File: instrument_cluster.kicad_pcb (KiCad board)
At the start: 2 copper layers, 99.1 x 45.7 mm, 82 parts, among them J1 Conn_02x16_Top_Bottom, J2 Conn_02x16_Top_Bottom, J3 USB mini-B SMD, J4 NOT_FITTED_SWD_Conn_01x04_Male, J5 54819-0572, J6 NOT_FITTED_SWD_Conn_01x04_Male, U1 LM2575S-5.0_NOPB, U10 74HC4050D, U11 TJA1040T, U12 TJA1040T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

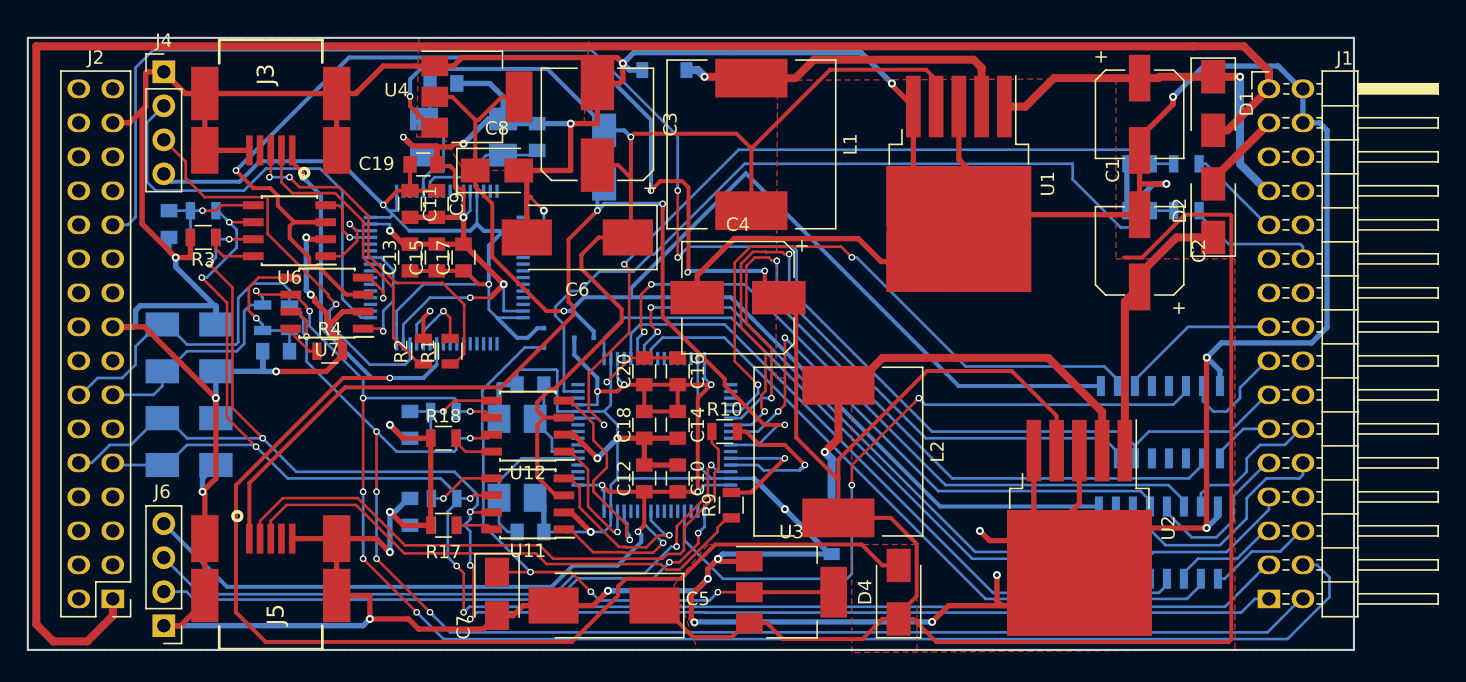
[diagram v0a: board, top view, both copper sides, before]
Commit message: fix signal trace length usb module A
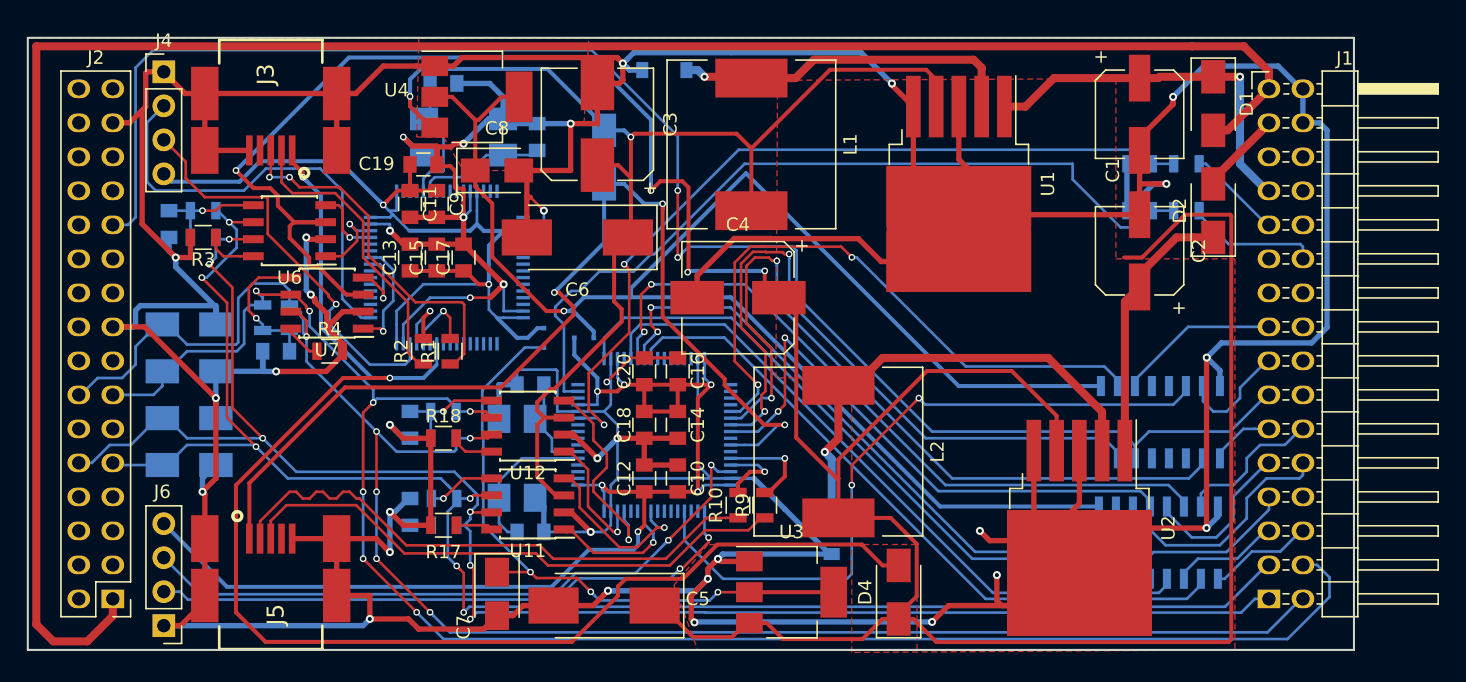
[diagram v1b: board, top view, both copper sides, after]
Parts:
- moved R10 5.59 mm to (161.0, 120.0), turned to 90 degrees
- moved R9 2.50 mm to (163.0, 120.0)
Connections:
- net Net-(J3-Pad2) renamed /Module A (2can_filter)/module_a_usb_D-
- net Net-(J3-Pad3) renamed /Module A (2can_filter)/module_a_usb_D+
- net Net-(J5-Pad2) renamed module_a_usb_D-
- net Net-(J5-Pad3) renamed module_a_usb_D+
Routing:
- net /Module B (2can_filter+extra)/USB_D-: track 13.5 -> 5.78 mm
- net module_a_usb_D-: track 46.0 -> 42.1 mm
- net /+5V_CAN-B: track 96.0 -> 92.7 mm
- net module_a_usb_D+: track 40.0 -> 42.0 mm
- net /Module B (2can_filter+extra)/USB_D+: track 9.11 -> 7.40 mm
- net /Module B (2can_filter+extra)/CAN2_TX: track 11.4 -> 10.3 mm
- net /USB_Vbus-B: track 75.6 -> 76.5 mm
- net /Module B (2can_filter+extra)/CAN2_RX: track 13.8 -> 13.0 mm
- net /Module B (2can_filter+extra)/SWCLK: track 44.5 -> 45.2 mm
- net /Module B (2can_filter+extra)/SWDIO: track 49.7 -> 49.1 mm
- net GND: vias 36 -> 35

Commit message: sch&pcb: add LED`s and refresh readme image`s
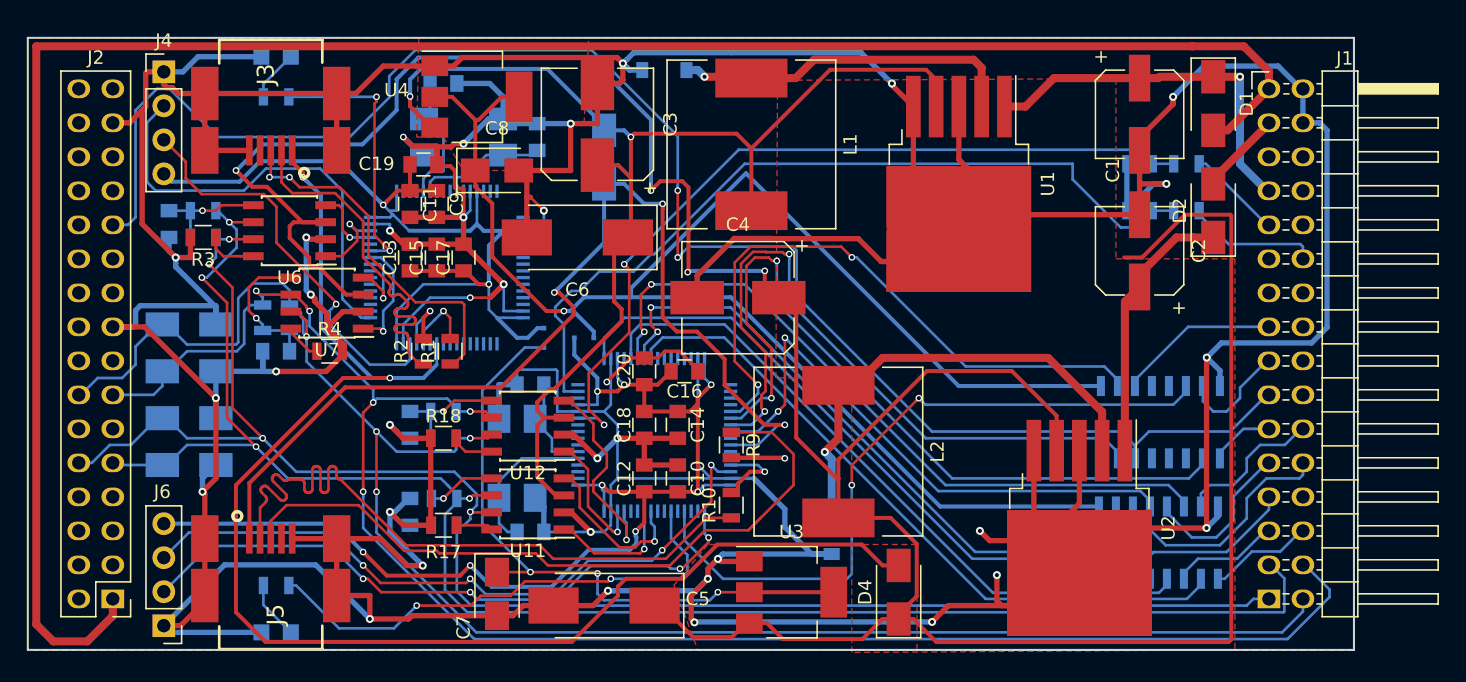
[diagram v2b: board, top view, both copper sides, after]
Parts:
- added D13: LED, LEDs:LED_0805, B.Cu at (126.5, 86.5)
- added D14: LED, LEDs:LED_0805, B.Cu at (126.5, 129.5)
- added R15: 1k, Resistors_SMD:R_0805, B.Cu at (126.5, 89.5)
- added R16: 10k, Resistors_SMD:R_0805, B.Cu at (126.5, 126.0)
- moved R9 5.15 mm to (160.5, 115.5), turned to 270 degrees
- moved C16 0.50 mm to (157.0, 110.0), turned to 0 degrees
- moved R10 0.50 mm to (160.5, 120.0)
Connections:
- net module_a_usb_D+ renamed Net-(J5-Pad3)
- net module_a_usb_D- renamed Net-(J5-Pad2)
- U5 pad 59: Net-(U5-Pad59) -> /Module A (2can_filter)/led_1
- U9 pad 54: Net-(U9-Pad54) -> /Module B (2can_filter+extra)/led_2
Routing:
- net /Module B (2can_filter+extra)/led_2: track 0.00 -> 37.9 mm, vias 0 -> 2
- net GND: track 665.1 -> 689.2 mm
- net /Module A (2can_filter)/led_1: track 0.00 -> 20.0 mm, vias 0 -> 2
- net Net-(J5-Pad3): track 42.0 -> 54.2 mm
- net Net-(J5-Pad2): track 42.1 -> 53.6 mm
- net /Module A (2can_filter)/module_a_usb_D-: track 22.4 -> 27.1 mm
- net Net-(D14-Pad2): track 0.00 -> 4.35 mm
- net /HS_CAN_L: track 125.1 -> 129.0 mm, vias 6 -> 4
- net Net-(D13-Pad2): track 0.00 -> 3.85 mm
- net /Module B (2can_filter+extra)/SWCLK: track 45.2 -> 48.1 mm, vias 2 -> 4
- net /ANTI-THEFT: track 121.0 -> 123.1 mm
- net /Module B (2can_filter+extra)/SWDIO: track 49.1 -> 51.1 mm, vias 2 -> 4
- net /MS_CAN_L: track 132.7 -> 130.8 mm, vias 7 -> 5
- net /+3V3_STM-B: track 91.8 -> 90.0 mm, vias 6 -> 8
- net /HS_CAN_H: track 125.8 -> 124.3 mm, vias 6 -> 4
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
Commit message: add gerbers files
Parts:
- J3, J5: footprint zulljon:USB_mini_B -> zpkl:USB_mini_B
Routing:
- net /+5V_CAN-A: track 223.5 -> 159.4 mm
- net /VBATT: track 151.1 -> 146.0 mm
- net /+3V3_LSH-B: track 121.6 -> 117.8 mm
- net GND: track 689.2 -> 691.9 mm, vias 35 -> 37
- net /+5V_CAN-B: track 92.7 -> 95.2 mm
- net /power_supply/+12V_A: track 20.3 -> 22.3 mm

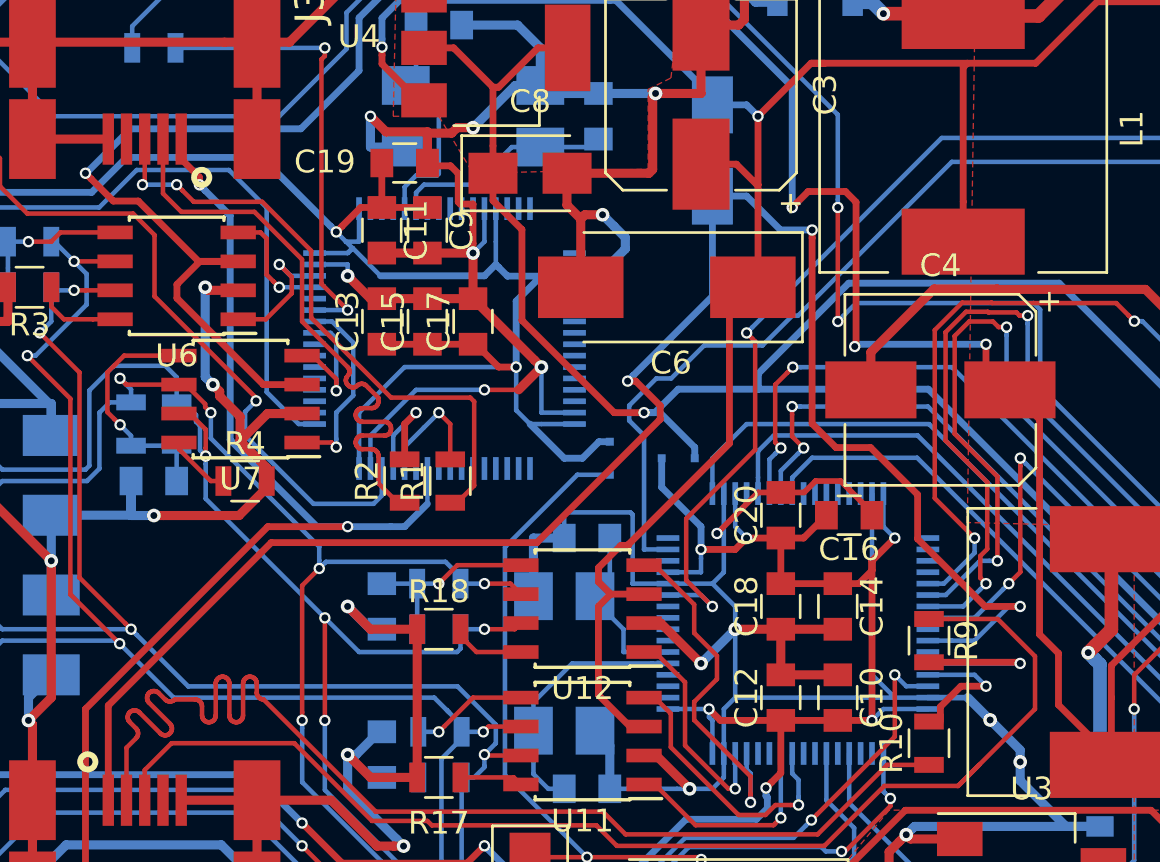
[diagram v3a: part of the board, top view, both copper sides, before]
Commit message: fix USB, swapped the traces D+ D-
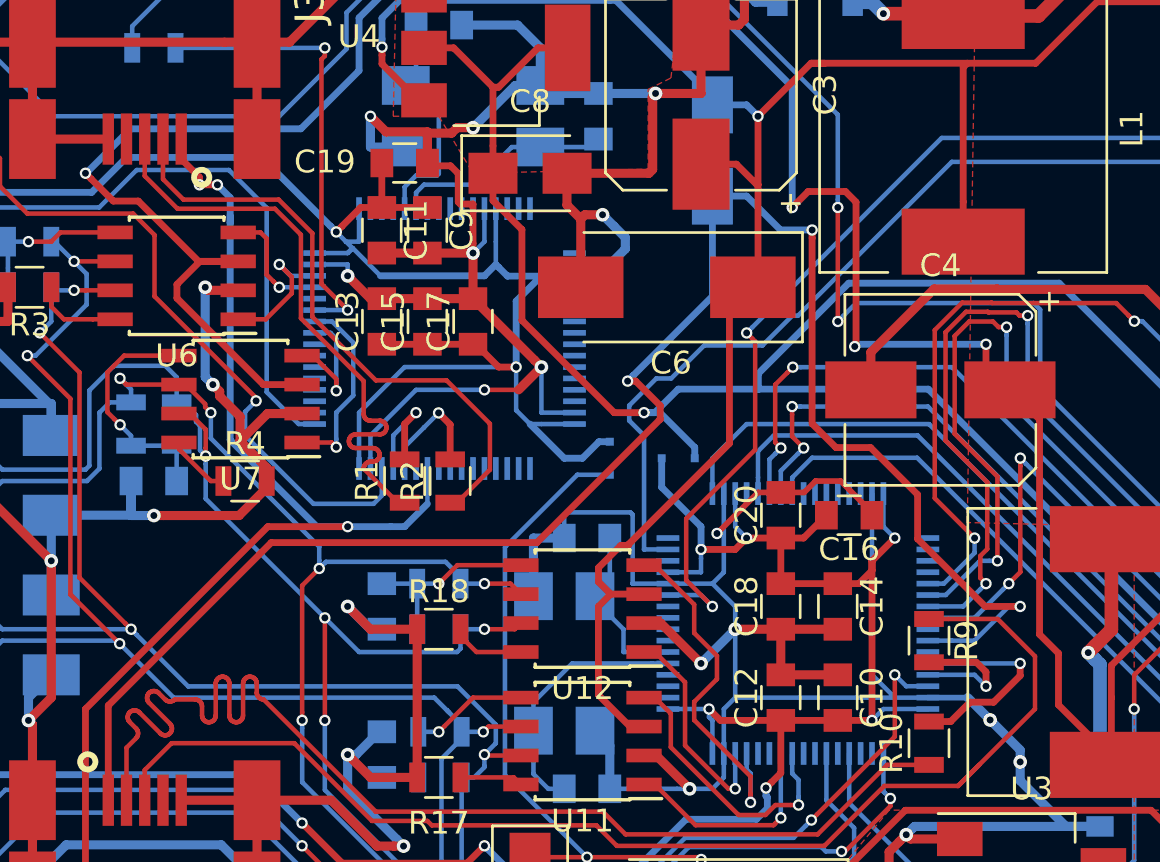
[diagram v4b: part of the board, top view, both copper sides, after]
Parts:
- moved R1 2.00 mm to (137.5, 108.5)
- moved R2 2.00 mm to (139.5, 108.5)
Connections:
- U5 pad 44: /Module A (2can_filter)/USB_D+ -> /Module A (2can_filter)/USB_D-
- U5 pad 45: /Module A (2can_filter)/USB_D- -> /Module A (2can_filter)/USB_D+
- U9 pad 44: /Module B (2can_filter+extra)/USB_D+ -> /Module B (2can_filter+extra)/USB_D-
- U9 pad 45: /Module B (2can_filter+extra)/USB_D- -> /Module B (2can_filter+extra)/USB_D+
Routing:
- net /Module B (2can_filter+extra)/USB_D-: track 5.78 -> 9.42 mm
- net /Module B (2can_filter+extra)/USB_D+: track 8.07 -> 6.06 mm
- net /USB_Vbus-A: track 104.8 -> 105.5 mm, vias 2 -> 3
- net /Module A (2can_filter)/module_a_usb_D+: track 27.3 -> 27.0 mm, vias 2 -> 0

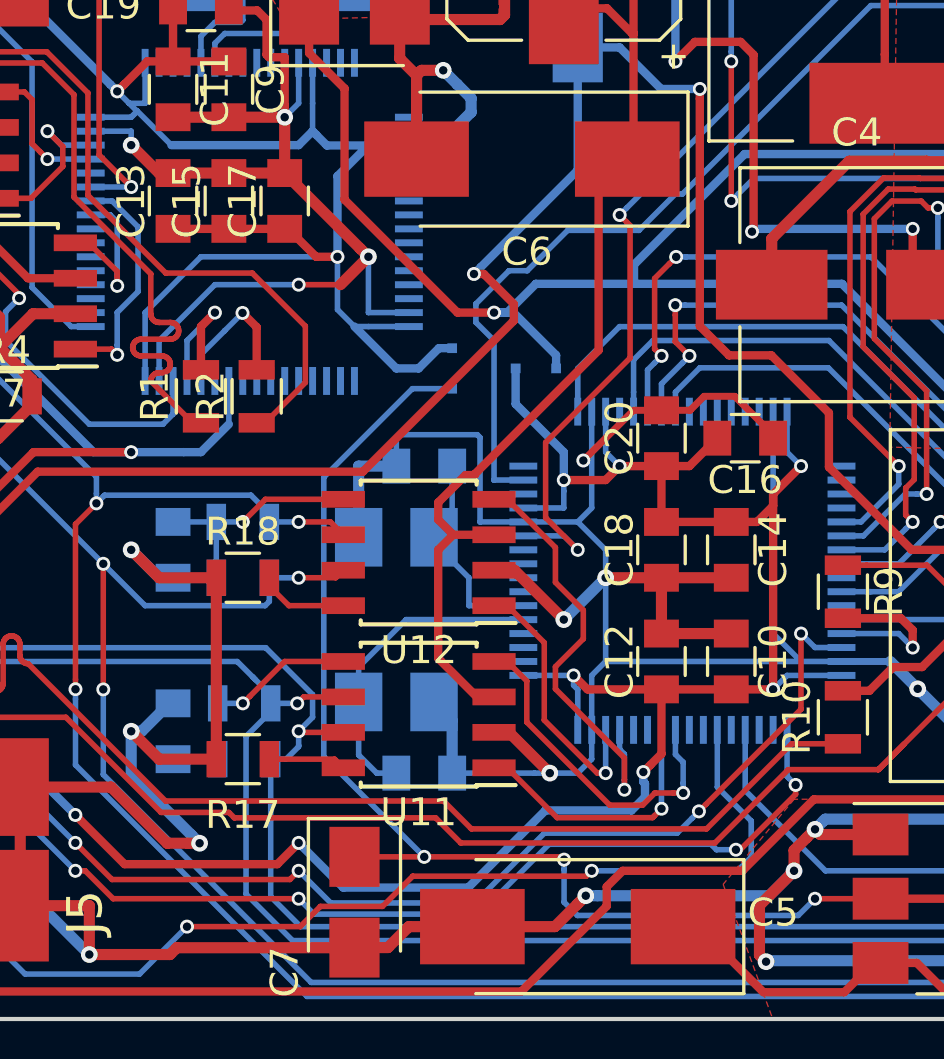
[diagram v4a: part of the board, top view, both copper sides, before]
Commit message: fix CAN, swapped the stm->to->can connection in module B
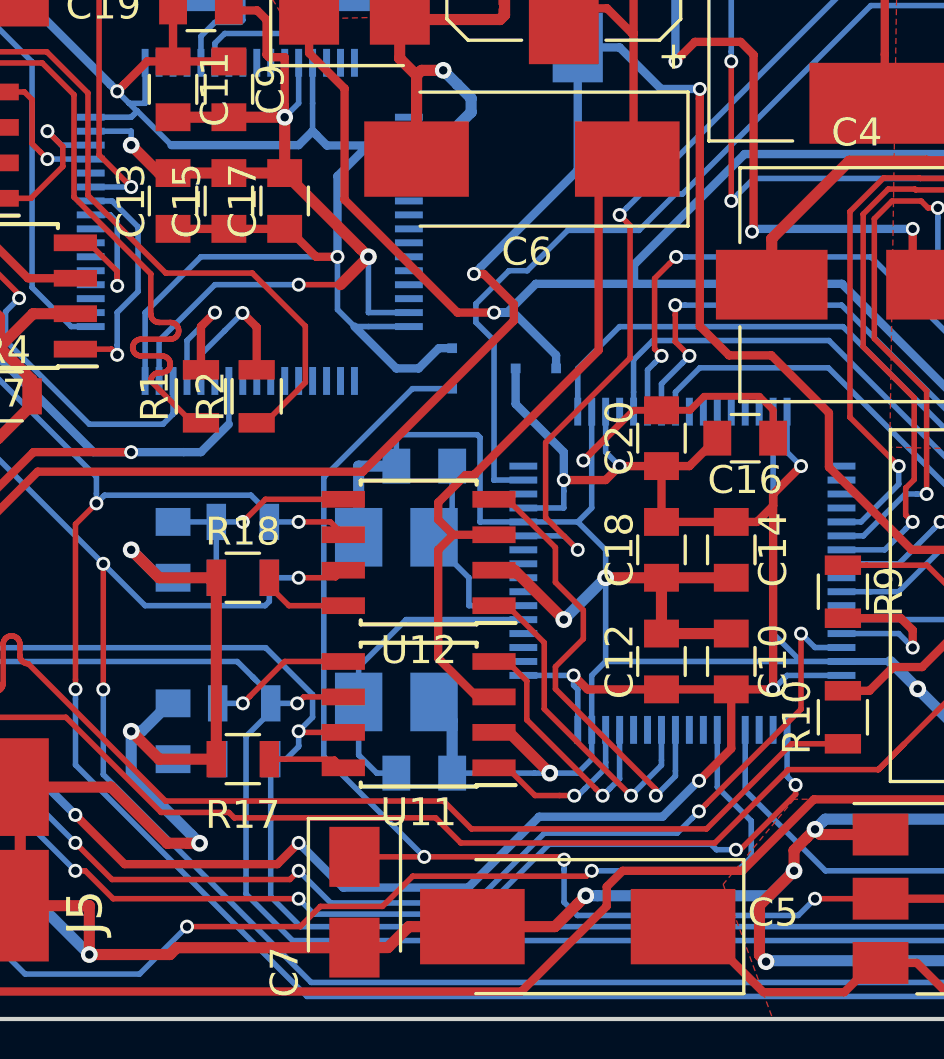
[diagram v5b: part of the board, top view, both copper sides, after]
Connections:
- net /Module A (2can_filter)/CAN1_RX renamed /Module A (2can_filter)/CAN_HS_RX
- net /Module A (2can_filter)/CAN1_TX renamed /Module A (2can_filter)/CAN_HS_TX
- net /Module A (2can_filter)/CAN2_RX renamed /Module A (2can_filter)/CAN_MS_RX
- net /Module A (2can_filter)/CAN2_TX renamed /Module A (2can_filter)/CAN_MS_TX
- U11 pad 1: /Module B (2can_filter+extra)/CAN2_TX -> /Module B (2can_filter+extra)/CAN_HS_TX
- U11 pad 4: /Module B (2can_filter+extra)/CAN2_RX -> /Module B (2can_filter+extra)/CAN_HS_RX
- U12 pad 1: /Module B (2can_filter+extra)/CAN1_TX -> /Module B (2can_filter+extra)/CAN_MS_TX
- U12 pad 4: /Module B (2can_filter+extra)/CAN1_RX -> /Module B (2can_filter+extra)/CAN_MS_RX
- U9 pad 57: /Module B (2can_filter+extra)/CAN2_RX -> /Module B (2can_filter+extra)/CAN_MS_RX
- U9 pad 58: /Module B (2can_filter+extra)/CAN2_TX -> /Module B (2can_filter+extra)/CAN_MS_TX
- U9 pad 61: /Module B (2can_filter+extra)/CAN1_RX -> /Module B (2can_filter+extra)/CAN_HS_RX
- U9 pad 62: /Module B (2can_filter+extra)/CAN1_TX -> /Module B (2can_filter+extra)/CAN_HS_TX
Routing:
- net /Module B (2can_filter+extra)/CAN_MS_RX: track 0.00 -> 16.8 mm, vias 0 -> 1
- net /Module B (2can_filter+extra)/CAN1_RX: track 15.7 -> 0.00 mm, vias 1 -> 0
- net /Module B (2can_filter+extra)/CAN2_RX: track 12.3 -> 0.00 mm, vias 1 -> 0
- net /Module B (2can_filter+extra)/CAN_MS_TX: track 0.00 -> 11.9 mm, vias 0 -> 1
- net /Module B (2can_filter+extra)/CAN2_TX: track 9.70 -> 0.00 mm, vias 1 -> 0
- net /Module B (2can_filter+extra)/CAN1_TX: track 9.66 -> 0.00 mm, vias 1 -> 0
- net /Module B (2can_filter+extra)/CAN_HS_RX: track 0.00 -> 9.31 mm, vias 0 -> 1
- net /Module B (2can_filter+extra)/CAN_HS_TX: track 0.00 -> 6.19 mm, vias 0 -> 1
- net /+3V3_STM-B: track 90.0 -> 91.8 mm
- net GND: track 691.9 -> 692.9 mm
